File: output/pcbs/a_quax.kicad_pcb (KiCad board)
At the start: 2 copper layers, 101.8 x 95.1 mm, 37 parts

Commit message: restructure code
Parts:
- D1, D10, D11, D12, D13, D14, D15, D16, D17, D2, D3, D4, D5, D6, D7, D8, D9: footprint ComboDiode -> diode
- MCU1: footprint xiao-ble-tht -> xiao-ble
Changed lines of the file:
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@@
             (pad 2 thru_hole circle (at -0 -5.9) (size 2.032 2.032) (drill 1.27) (layers *.Cu *.Mask) (net 2 "P2"))
           )
-        (footprint "ComboDiode" (layer "F.Cu")
+        (footprint "diode" (layer "F.Cu")
         (at 13.4259428 -4.5192472 12)
         (attr through_hole)
@@
             (pad 2 thru_hole circle (at -0 -5.9) (size 2.032 2.032) (drill 1.27) (layers *.Cu *.Mask) (net 2 "P2"))
           )
-        (footprint "ComboDiode" (layer "F.Cu")
+        (footprint "diode" (layer "F.Cu")
         (at 9.891444 -21.1477564 12)
         (attr through_hole)
@@
             (pad 2 thru_hole circle (at -0 -5.9) (size 2.032 2.032) (drill 1.27) (layers *.Cu *.Mask) (net 2 "P2"))
           )
-        (footprint "ComboDiode" (layer "F.Cu")
+        (footprint "diode" (layer "F.Cu")
         (at 6.3569453 -37.7762656 12)
         (attr through_hole)
@@
             (pad 2 thru_hole circle (at -0 -5.9) (size 2.032 2.032) (drill 1.27) (layers *.Cu *.Mask) (net 9 "P3"))
           )
-        (footprint "ComboDiode" (layer "F.Cu")
+        (footprint "diode" (layer "F.Cu")
         (at 31.1942902 -20.396465 5)
         (attr through_hole)
@@
             (pad 2 thru_hole circle (at -0 -5.9) (size 2.032 2.032) (drill 1.27) (layers *.Cu *.Mask) (net 9 "P3"))
           )
-        (footprint "ComboDiode" (layer "F.Cu")
+        (footprint "diode" (layer "F.Cu")
         (at 29.7126425 -37.3317749 5)
         (attr through_hole)
@@
             (pad 2 thru_hole circle (at -0 -5.9) (size 2.032 2.032) (drill 1.27) (layers *.Cu *.Mask) (net 9 "P3"))
           )
-        (footprint "ComboDiode" (layer "F.Cu")
+        (footprint "diode" (layer "F.Cu")
         (at 28.230995 -54.2670848 5)
         (attr through_hole)
@@
             (pad 2 thru_hole circle (at -0 -5.9) (size 2.032 2.032) (drill 1.27) (layers *.Cu *.Mask) (net 13 "P4"))
           )
-        (footprint "ComboDiode" (layer "F.Cu")
+        (footprint "diode" (layer "F.Cu")
         (at 50.7493385 -27.6940883 0)
         (attr through_hole)
@@
             (pad 2 thru_hole circle (at -0 -5.9) (size 2.032 2.032) (drill 1.27) (layers *.Cu *.Mask) (net 13 "P4"))
           )
-        (footprint "ComboDiode" (layer "F.Cu")
+        (footprint "diode" (layer "F.Cu")
         (at 50.7493386 -44.6940883 0)
         (attr through_hole)
@@
             (pad 2 thru_hole circle (at -0 -5.9) (size 2.032 2.032) (drill 1.27) (layers *.Cu *.Mask) (net 13 "P4"))
           )
-        (footprint "ComboDiode" (layer "F.Cu")
+        (footprint "diode" (layer "F.Cu")
         (at 50.7493386 -61.6940884 0)
         (attr through_hole)
@@
             (pad 2 thru_hole circle (at -0 -5.9) (size 2.032 2.032) (drill 1.27) (layers *.Cu *.Mask) (net 17 "P5"))
           )
-        (footprint "ComboDiode" (layer "F.Cu")
+        (footprint "diode" (layer "F.Cu")
         (at 68.5493385 -22.0274216 0)
         (attr through_hole)
@@
             (pad 2 thru_hole circle (at -0 -5.9) (size 2.032 2.032) (drill 1.27) (layers *.Cu *.Mask) (net 17 "P5"))
           )
-        (footprint "ComboDiode" (layer "F.Cu")
+        (footprint "diode" (layer "F.Cu")
         (at 68.5493385 -39.0274216 0)
         (attr through_hole)
@@
             (pad 2 thru_hole circle (at -0 -5.9) (size 2.032 2.032) (drill 1.27) (layers *.Cu *.Mask) (net 17 "P5"))
           )
-        (footprint "ComboDiode" (layer "F.Cu")
+        (footprint "diode" (layer "F.Cu")
         (at 68.5493386 -56.0274217 0)
         (attr through_hole)
@@
             (pad 2 thru_hole circle (at -0 -5.9) (size 2.032 2.032) (drill 1.27) (layers *.Cu *.Mask) (net 21 "P6"))
           )
-        (footprint "ComboDiode" (layer "F.Cu")
+        (footprint "diode" (layer "F.Cu")
         (at 86.5493385 -19.1940883 0)
         (attr through_hole)
@@
             (pad 2 thru_hole circle (at -0 -5.9) (size 2.032 2.032) (drill 1.27) (layers *.Cu *.Mask) (net 21 "P6"))
           )
-        (footprint "ComboDiode" (layer "F.Cu")
+        (footprint "diode" (layer "F.Cu")
         (at 86.5493385 -36.1940884 0)
         (attr through_hole)
@@
             (pad 2 thru_hole circle (at -0 -5.9) (size 2.032 2.032) (drill 1.27) (layers *.Cu *.Mask) (net 21 "P6"))
           )
-        (footprint "ComboDiode" (layer "F.Cu")
+        (footprint "diode" (layer "F.Cu")
         (at 86.5493385 -53.1940883 0)
         (attr through_hole)
@@
             (pad 2 thru_hole circle (at -0 -5.9) (size 2.032 2.032) (drill 1.27) (layers *.Cu *.Mask) (net 17 "P5"))
           )
-        (footprint "ComboDiode" (layer "F.Cu")
+        (footprint "diode" (layer "F.Cu")
         (at 69.245204 -1.1454286000000007 -8)
         (attr through_hole)
@@
             (pad 2 thru_hole circle (at -0 -5.9) (size 2.032 2.032) (drill 1.27) (layers *.Cu *.Mask) (net 21 "P6"))
           )
-        (footprint "ComboDiode" (layer "F.Cu")
+        (footprint "diode" (layer "F.Cu")
         (at 89.1798617 3.4568497000000002 -18)
         (attr through_hole)
@@
         (pad 2 smd rect (at 1.65 0 -18) (size 0.9 1.2) (layers "B.Cu" "B.Paste" "B.Mask") (net 26 "second_only"))
         (pad 2 thru_hole circle (at 1.65 0 -18) (size 0.6 0.6) (drill 0.3) (layers *.Cu *.Mask) (net 26 "second_only")))
-        (footprint "xiao-ble-tht" (layer "F.Cu")
+        (footprint "xiao-ble" (layer "F.Cu")
         (at 20.1642069 17.5623242 102)
         (attr smd exclude_from_pos_files)

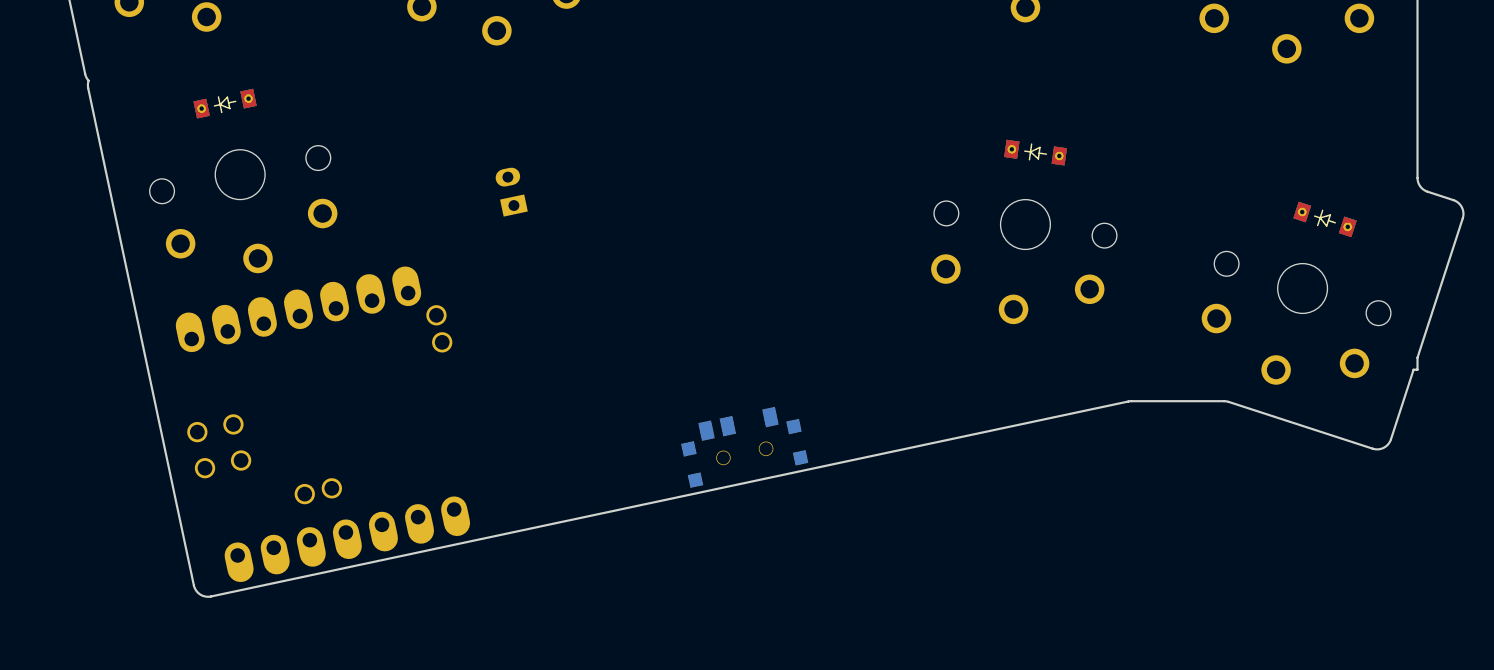
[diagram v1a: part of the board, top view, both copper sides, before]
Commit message: experimental mcu placement
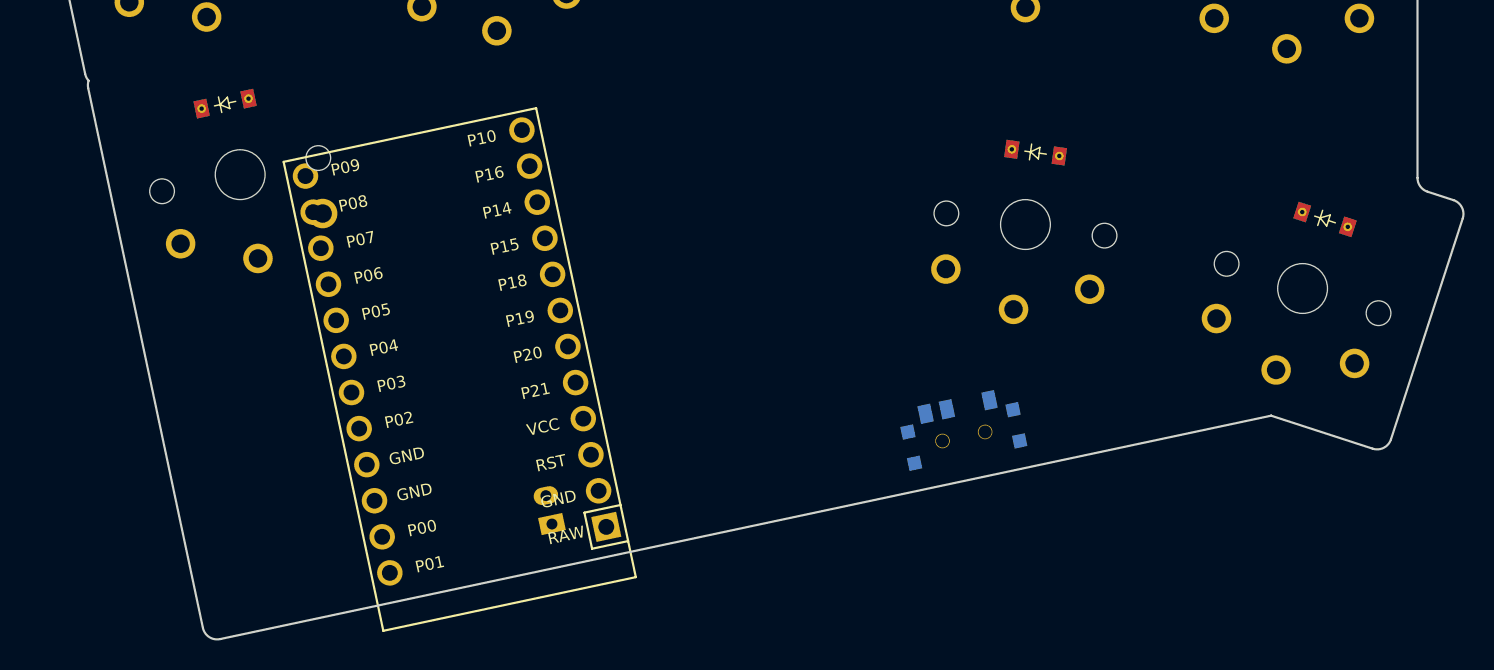
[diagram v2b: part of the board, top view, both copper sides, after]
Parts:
- MCU1: footprint xiao-ble -> ProMicro
- moved JST1 22.1 mm to (35.7, 23.5)
- moved T1 15.1 mm to (64.3, 18.4)
- moved MCU1 10.4 mm to (29.3, 12.5)
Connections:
- net CLK renamed P18
- net NFC0 renamed P14
- net NFC1 renamed P16
- MCU1 pad 1: VCC5 -> RAW
- MCU1 pad 12: P6 -> P10
- MCU1 pad 13: P5 -> P1
- MCU1 pad 14: P4 -> P0
- MCU1 pad 15: P3 -> GND
- MCU1 pad 16: P2 -> GND
- MCU1 pad 17: P1 -> P2
- MCU1 pad 18: P0 -> P3
- MCU1 pad 19: DIO -> P4
- MCU1 pad 20: RST -> P5
- MCU1 pad 21: RAW -> P6
- MCU1 pad 22: GND -> P7
- MCU1 pad 3: VCC3 -> RST
- MCU1 pad 4: P10 -> VCC
- MCU1 pad 5: P9 -> P21
- MCU1 pad 6: P8 -> P20
- MCU1 pad 7: P7 -> P19
- MCU1 pad 9: GND -> P15
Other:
- board size 101.8 x 95.1 mm -> 101.8 x 98.1 mm

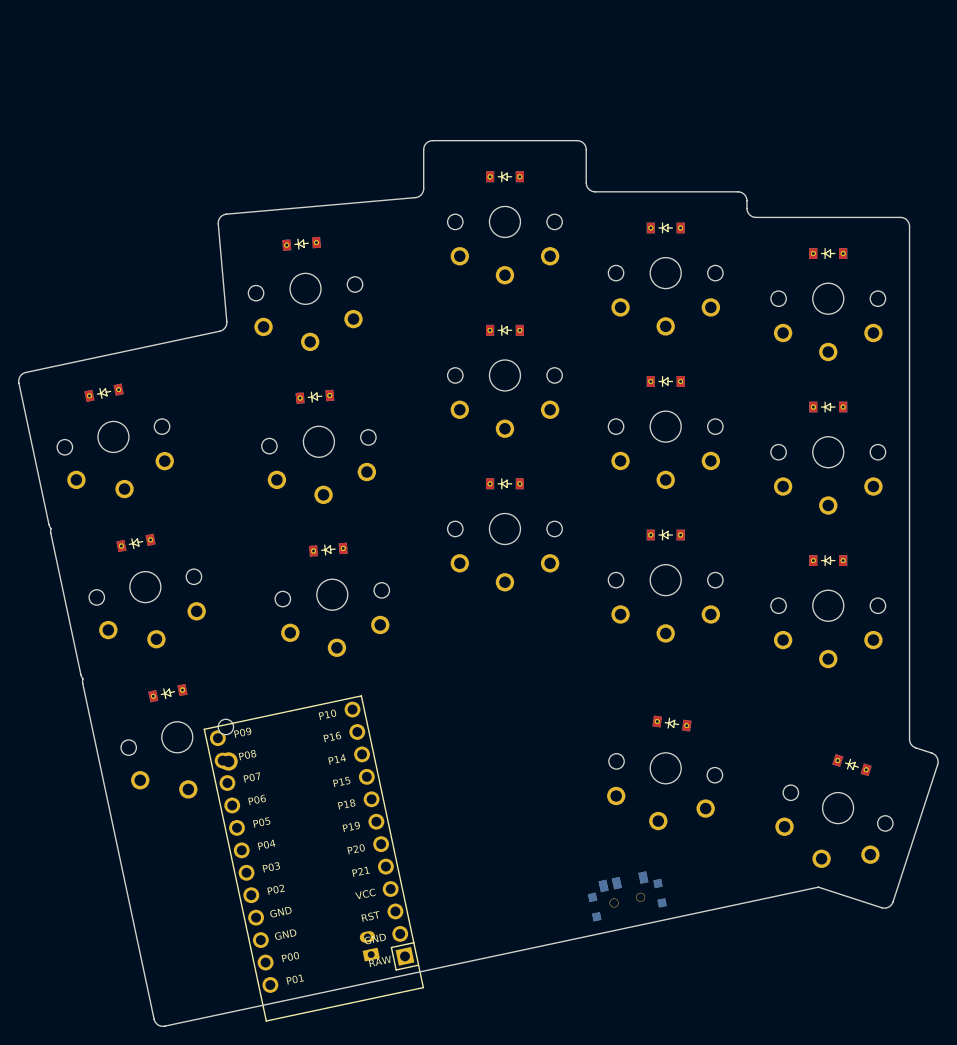
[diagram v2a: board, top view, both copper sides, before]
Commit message: moving mcu around to find the best place for it.
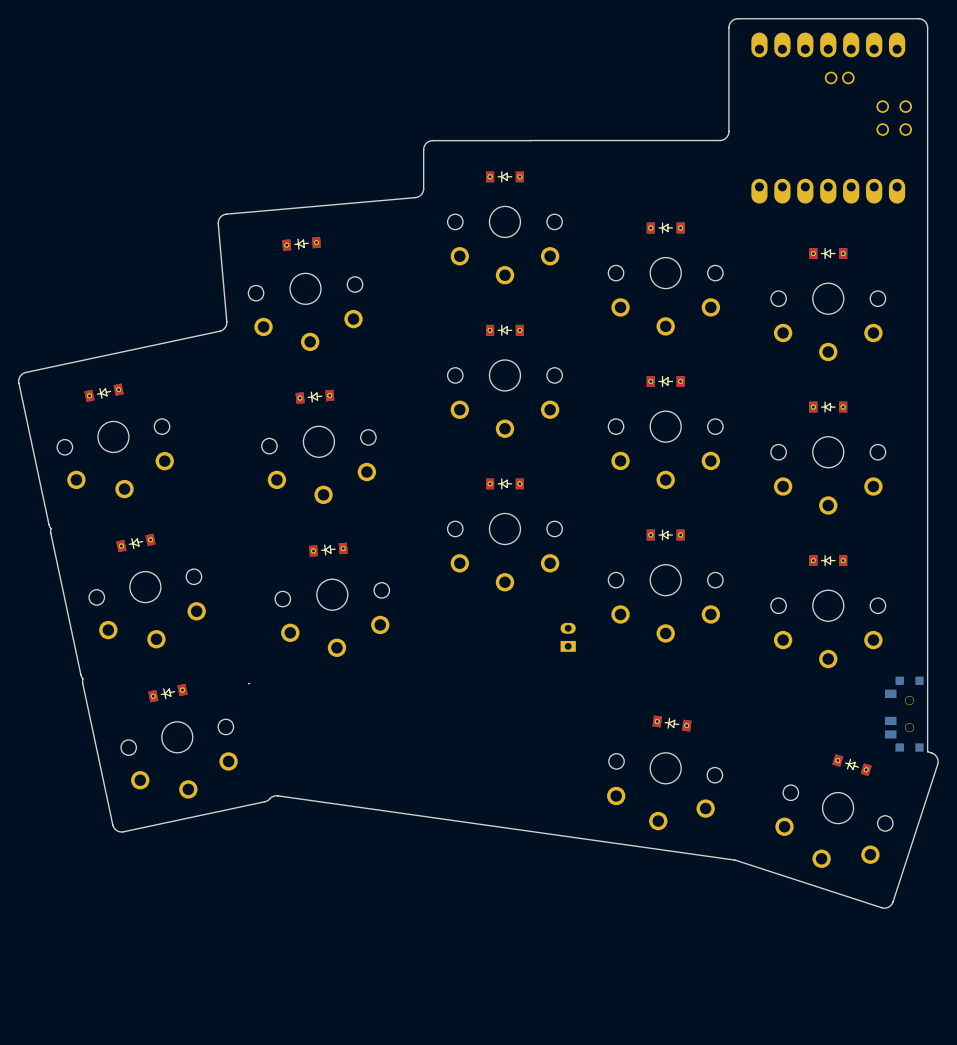
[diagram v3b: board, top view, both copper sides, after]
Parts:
- MCU1: footprint ProMicro -> xiao-ble
- moved MCU1 99.0 mm to (86.5, -68.2), turned to -90 degrees
- moved JST1 40.6 mm to (57.7, -10.7), turned to -90 degrees
- moved T1 37.4 mm to (95.5, -2.19), turned to -90 degrees
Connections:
- net P18 renamed CLK
- MCU1 pad 1: RAW -> VCC5
- MCU1 pad 12: P10 -> P6
- MCU1 pad 13: P1 -> P5
- MCU1 pad 14: P0 -> P4
- MCU1 pad 15: GND -> P3
- MCU1 pad 16: GND -> P2
- MCU1 pad 17: P2 -> P1
- MCU1 pad 18: P3 -> P0
- MCU1 pad 19: P4 -> DIO
- MCU1 pad 20: P5 -> RST
- MCU1 pad 21: P6 -> RAW
- MCU1 pad 22: P7 -> GND
- MCU1 pad 3: RST -> VCC3
- MCU1 pad 4: VCC -> P10
- MCU1 pad 5: P21 -> P9
- MCU1 pad 6: P20 -> P8
- MCU1 pad 7: P19 -> P7
- MCU1 pad 9: P15 -> GND
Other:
- board size 101.8 x 98.1 mm -> 101.8 x 98.5 mm
